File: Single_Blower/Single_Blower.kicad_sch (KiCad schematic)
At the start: 10 parts, among them J1 BLOWER 1, J3 LED 1, U2 5V

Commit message: Adding in connectors
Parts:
- added C1: 0.1uF, Switch_Daughter_Card_ftp:C0805, symbol Device:C_Small
- added J2: SWITCH, symbol Connector_Generic:Conn_01x02
- added J4: Conn_01x03, symbol Connector_Generic:Conn_01x03
- added R1: 10k, Switch_Daughter_Card_ftp:R0805, symbol Device:R_US
- J1: value BLOWER 1 -> BLOWER; footprint Fan_Daughter_footprints:4-pin-shrouded -> (none); Distributor PN A30926-ND -> A1927-ND; Mfg. PN 2-644803-4 -> 640457-4
- J3: value LED 1 -> LED; footprint Fan_Daughter_footprints:2-pin-shrouded -> (none); Distributor PN A30924-ND -> A1926-ND; Mfg. PN 2-644803-2 -> 640457-2
- R2: value 10k -> 100k; footprint Fan_Daughter_footprints:R0805 -> Switch_Daughter_Card_ftp:R0805; Distributor PN RMCF0805FT10K0TR-ND -> RMCF0805FG100KTR-ND; Mfg. PN RMCF0805FT10K0 -> RMCF0805FG100K
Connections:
- net +5V: now also R1.1; no longer R2.1
- net GND: now also C1.2, J2.2 (Pin_2)
- net PIN_1_Tach: no longer names the net of R2.2
- net PIN_1_Tach: now also J2.1 (Pin_1), R1.2; no longer J1.3 (Pin_3)
- new net SW_1: C1.1, R2.1
- no-connect marks 0 -> 1
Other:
- note added: "https://protosupplies.com/product/e18-d80nk-adjustable-infrared-proximity-sensor-module/"

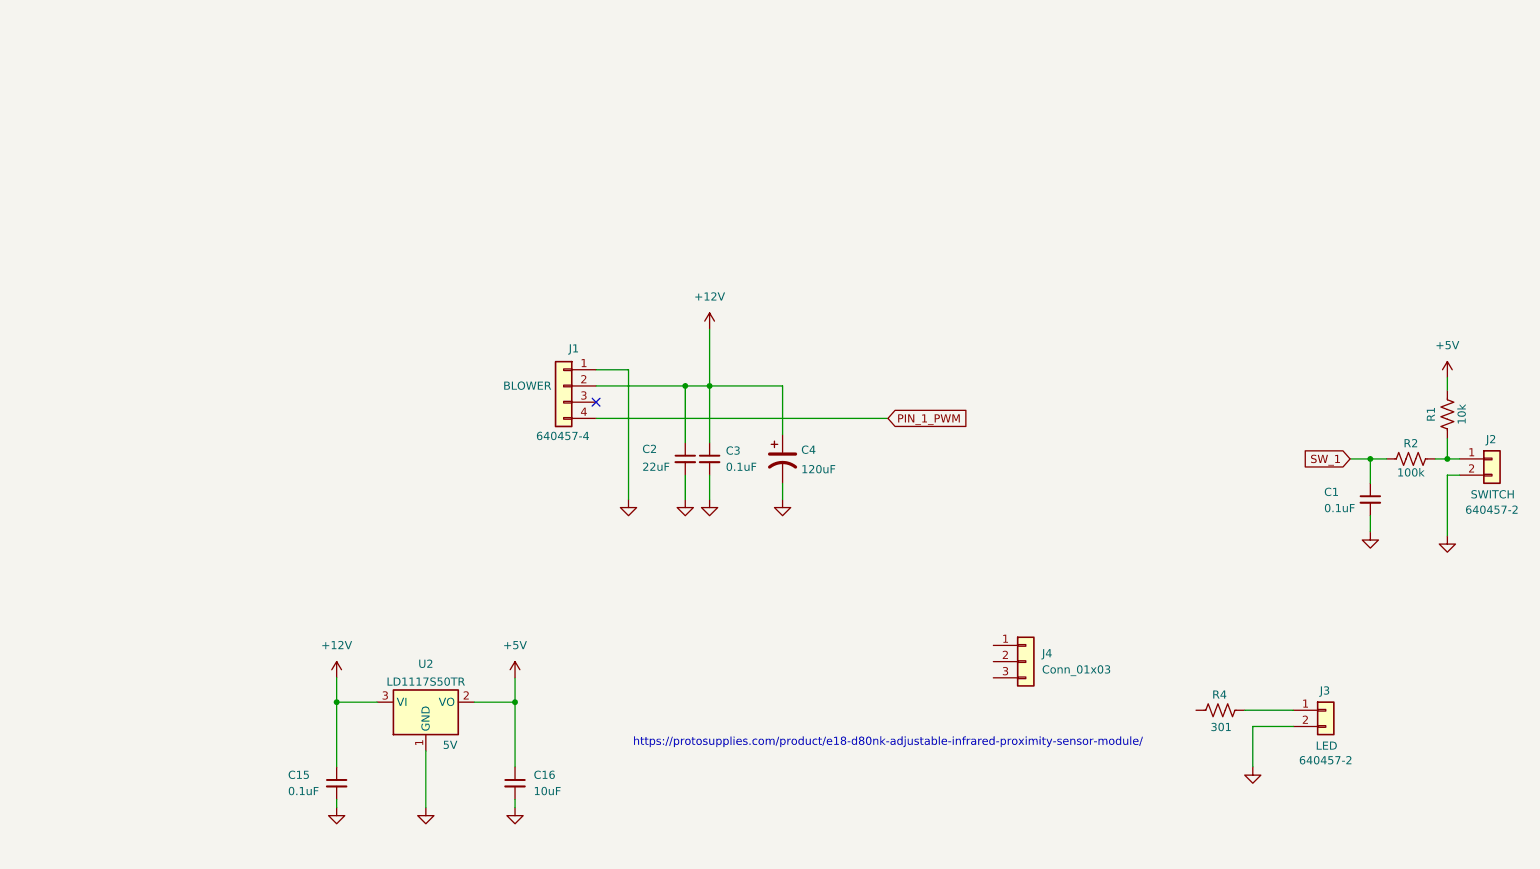
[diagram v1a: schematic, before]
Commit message: Finalized schematic on blower card
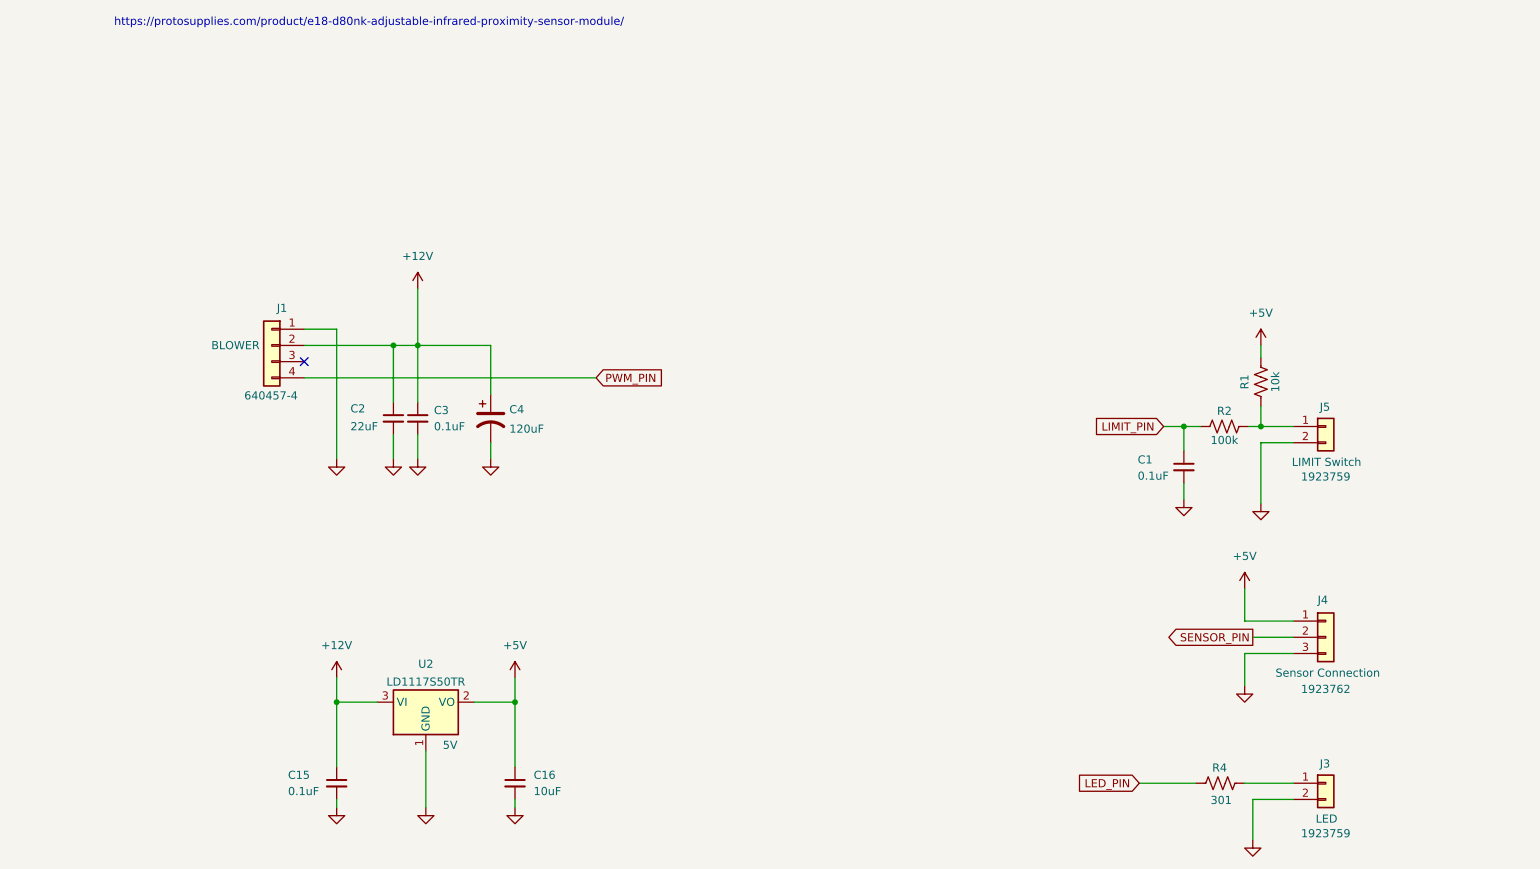
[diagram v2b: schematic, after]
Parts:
- removed J2: SWITCH, symbol Connector_Generic:Conn_01x02
- added J5: LIMIT Switch, Single_blower_footprints:PHOENIX_1923759, symbol Connector_Generic:Conn_01x02
- J3: footprint (none) -> Single_blower_footprints:PHOENIX_1923759; Distributor PN A1926-ND -> 277-14388-ND; Mfg. TE Connectivity AMP Connectors -> Phoenix Contact; Mfg. PN 640457-2 -> 1923759
- J4: value Conn_01x03 -> Sensor Connection; footprint (none) -> Single_blower_footprints:PHOENIX_1923762; Distributor (none) -> Digikey; Distributor PN (none) -> 277-14389-ND; Mfg, (none) -> Phoenix Contact; Mfg. PN (none) -> 1923762
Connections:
- net +5V: now also J4.1 (Pin_1)
- net GND: now also J4.3 (Pin_3), J5.2 (Pin_2)
- net at R1.2, R2.2: now also J5.1 (Pin_1)
- net LED_PIN: now reaches R4.1
- net SENSOR_PIN: now reaches J4.2 (Pin_2)
- net PIN_1_PWM renamed PWM_PIN
- net SW_1 renamed LIMIT_PIN
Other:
- moved on the sheet: C1, C2, C3, C4, J1, J3, J4, R1, R2, R4
